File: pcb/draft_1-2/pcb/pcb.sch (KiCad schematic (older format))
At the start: 35 parts, among them J1 USB4110-GF-A, J2 SWD, U1 H3LIS200DLTR, U2 ATSAML21J16B-AUT, U3 BQ25155

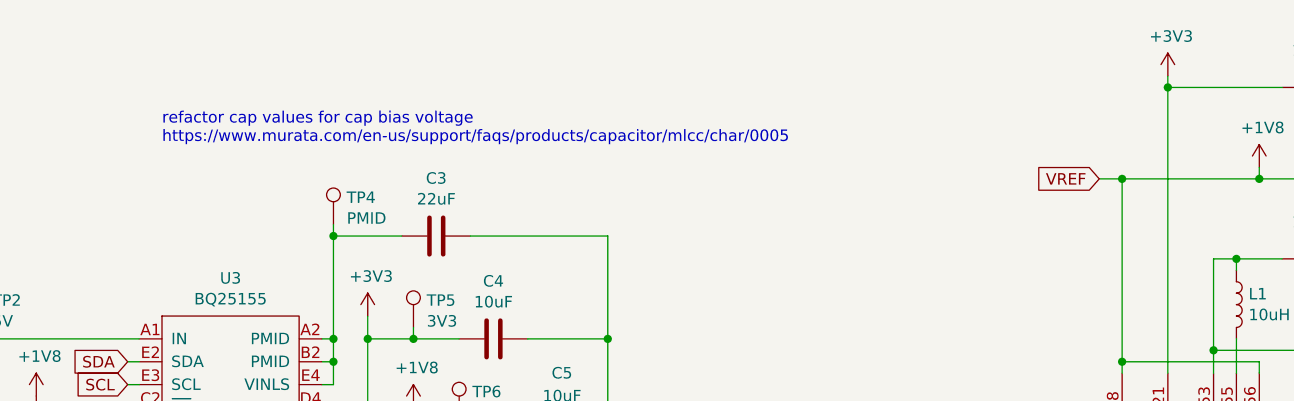
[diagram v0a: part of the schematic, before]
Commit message: add 2*3 100 mil header to BOM
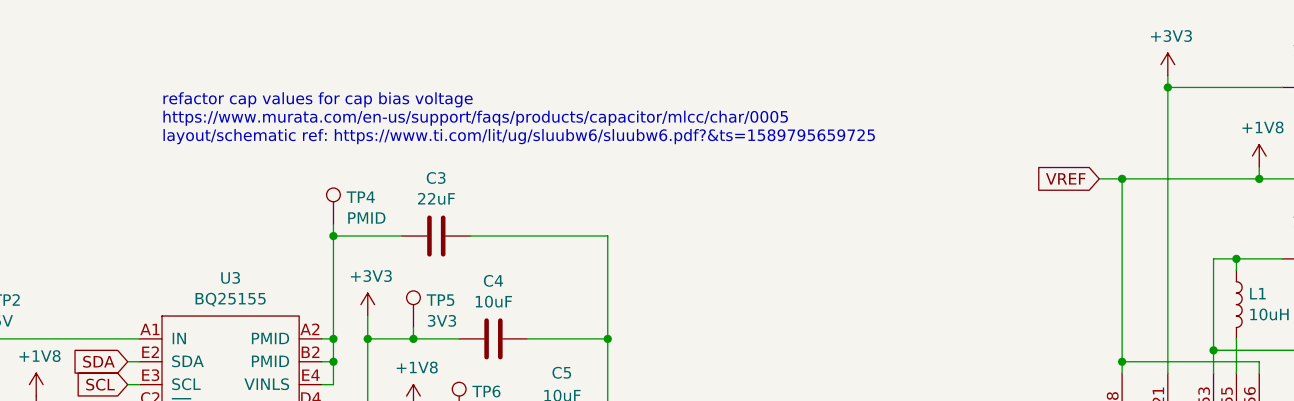
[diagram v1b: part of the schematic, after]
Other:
- note added: "refactor cap values for cap bias voltage\nhttps://www.murata.com/en-us/support/faqs/products/capacitor/mlcc/char/0005\nlayout/schematic ref: https://www.ti.com/lit/ug/sluubw6/sluubw6.pdf?&ts=1589795659725"
- note removed: "refactor cap values for cap bias voltage\nhttps://www.murata.com/en-us/support/faqs/products/capacitor/mlcc/char/0005"
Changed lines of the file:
@@
 	5050 2550 5250 2550
 Text Notes 4300 1100 0    50   ~ 0
-refactor cap values for cap bias voltage\nhttps://www.murata.com/en-us/support/faqs/products/capacitor/mlcc/char/0005
+refactor cap values for cap bias voltage\nhttps://www.murata.com/en-us/support/faqs/products/capacitor/mlcc/char/0005\nlayout/schematic ref: https://www.ti.com/lit/ug/sluubw6/sluubw6.pdf?&ts=1589795659725
 Text GLabel 3650 2550 0    50   Input ~ 0
 INT3
